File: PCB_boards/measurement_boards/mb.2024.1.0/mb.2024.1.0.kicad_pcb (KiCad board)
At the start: 2 copper layers, 247.8 x 124.2 mm, 119 parts, among them J1 DPS_out_12v_GND, J10 DPS+, J11 Screw_Terminal_VMN, J12 Conn_01x08_Socket, J13 Connector_I2C_for_mux, J14 Conn_01x02_Socket, J15 Conn_01x08_Socket, J16 RX_bat, J17 DPS GND, J18 ELEC_M, J19 ELEC_N, J2 DPS5005_input_0_to_50V, J20 shunt +, J21 shunt -, J22 Conn_01x04_Socket, J23 Conn_01x05_Socket, J24 Connector_I2C_for_MC, J25 Conn_01x04_Socket, J26 Conn_01x05_Socket, J27 Screw_Terminal_01x03, J3 Screw_Terminal_AB, J4 Conn_01x08_Socket, J5 Conn_01x04_Socket, J6 Conn_01x08_Socket, J7 Raspberry_Pi_2_3, J8 Connector_I2C_for_MCP23008, J9 TX_bat, K1 G5LE-1, K2 G5LE-1, K3 G5LE-1, K4 G5LE-1, K5 G5LE-1, K6 G5LE-1, K7 G5LE-1, Q1 ZVN4206ASTZ, Q2 ZVN4206ASTZ, Q3 ZVN4206ASTZ, Q4 ZVN4206ASTZ, Q5 ZVN4206ASTZ, Q6 ZVN4206ASTZ, Q7 ZVN4206ASTZ, U1 MCP23008-xP, U10 DG411xJ, U2 OP07, U4 1085, U5 1085, U6 OP07, U7 REF03GP, U8 MCP23008-xP, U9 OP07

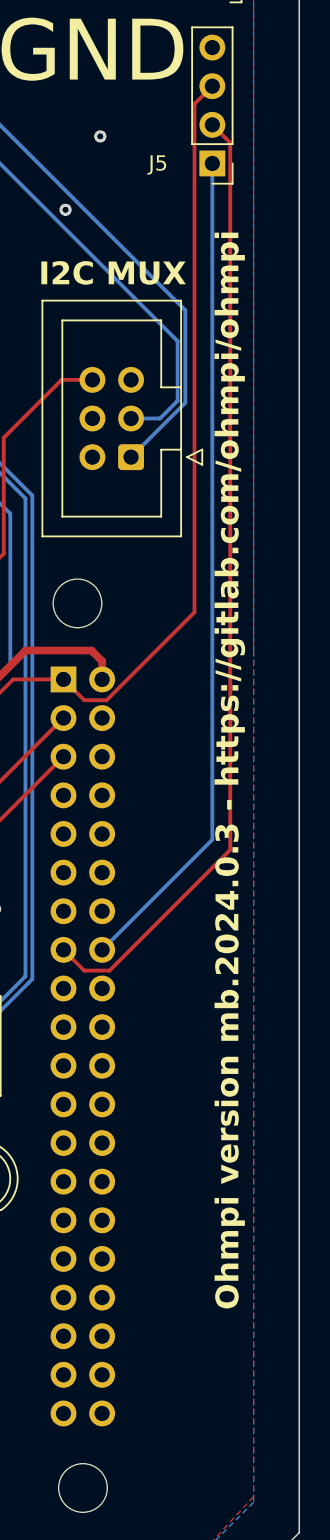
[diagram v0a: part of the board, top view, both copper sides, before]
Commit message: change name 2024.0.3 to 2024.1.0
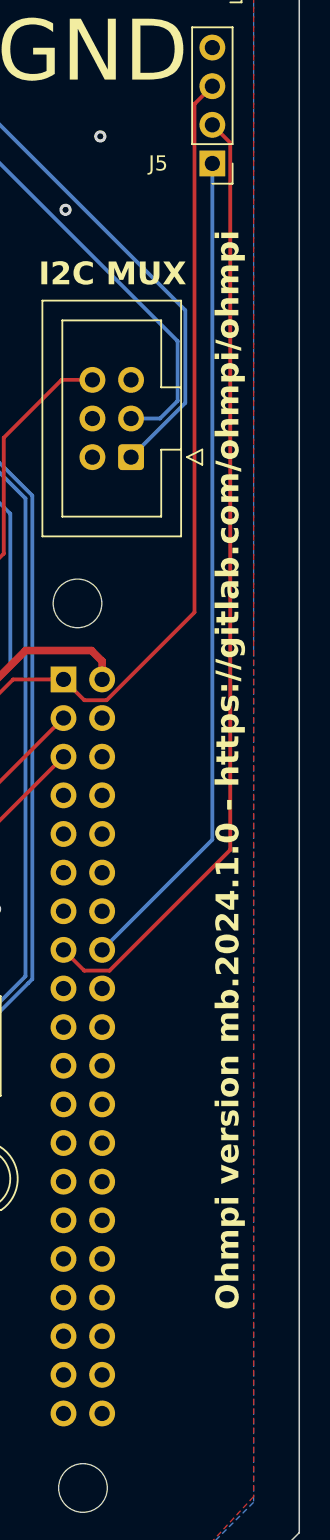
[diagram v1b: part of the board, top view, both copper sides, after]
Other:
- board text added: "Ohmpi version mb.2024.1.0 - https://gitlab.com/ohmpi/ohmpi"
- board text removed: "Ohmpi version mb.2024.0.3 - https://gitlab.com/ohmpi/ohmpi"
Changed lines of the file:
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@@
     (effects (font (size 4 4) (thickness 0.5)))
   )
-  (gr_text "Ohmpi version mb.2024.0.3 - https://gitlab.com/ohmpi/ohmpi" (at 257.302 101.854 90) (layer "F.SilkS")
+  (gr_text "Ohmpi version mb.2024.1.0 - https://gitlab.com/ohmpi/ohmpi" (at 257.302 101.854 90) (layer "F.SilkS")
     (effects (font (size 1.5 1.5) (thickness 0.3) bold))
   )

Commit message: update diode 1n4007
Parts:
- D1, D2, D3, D4, D7, D8, D9: value 1N4001 -> 1N4007
